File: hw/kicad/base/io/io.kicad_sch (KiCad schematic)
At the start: 13 parts, among them J1 SPI, J10 Conn_02x20_Odd_Even, J11 ADC 2, J12 UART1, J13 Conn_02x20_Odd_Even, J2 PWM, J3 UART2, J4 I2C, J5 PWM, J6 CAN, J7 PWM, J8 PWM, J9 ADC 1

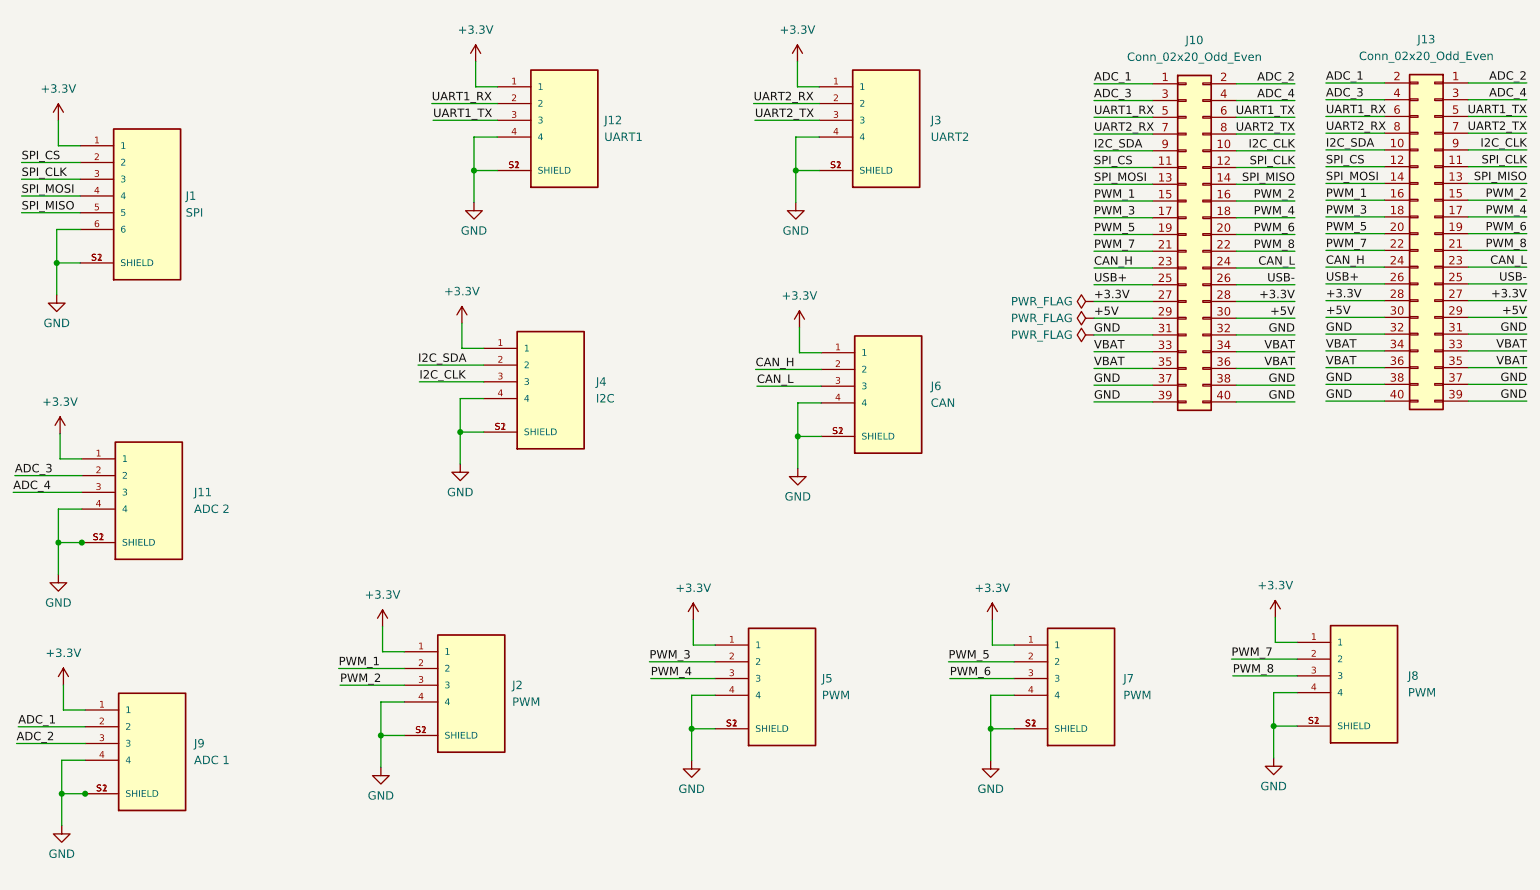
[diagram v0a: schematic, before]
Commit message: 新增陀螺仪小板子
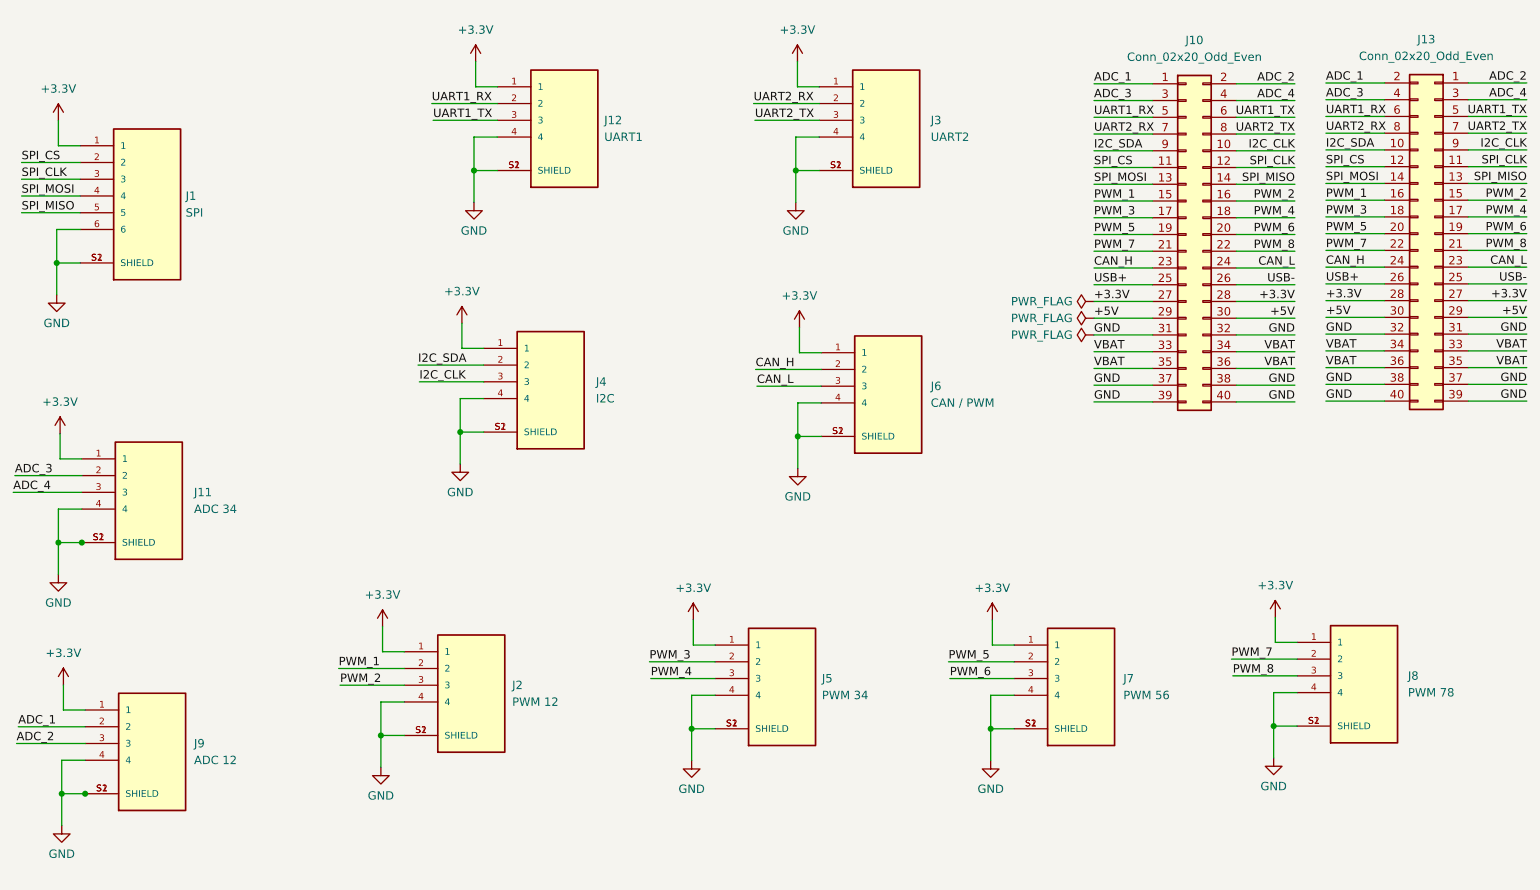
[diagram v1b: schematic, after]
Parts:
- J11: value ADC 2 -> ADC 34
- J2: value PWM -> PWM 12
- J5: value PWM -> PWM 34
- J6: value CAN -> CAN / PWM
- J7: value PWM -> PWM 56
- J8: value PWM -> PWM 78
- J9: value ADC 1 -> ADC 12
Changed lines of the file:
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@@
       (effects (font (size 1.27 1.27)) (justify left))
     )
-    (property "Value" "PWM" (at 158.75 144.5768 0)
+    (property "Value" "PWM 34" (at 158.75 144.5768 0)
       (effects (font (size 1.27 1.27)) (justify left))
     )
@@
       (effects (font (size 1.27 1.27)) (justify left))
     )
-    (property "Value" "ADC 1" (at 63.5 154.432 0)
+    (property "Value" "ADC 12" (at 63.5 154.432 0)
       (effects (font (size 1.27 1.27)) (justify left))
     )
@@
       (effects (font (size 1.27 1.27)) (justify left))
     )
-    (property "Value" "PWM" (at 204.47 144.5768 0)
+    (property "Value" "PWM 56" (at 204.47 144.5768 0)
       (effects (font (size 1.27 1.27)) (justify left))
     )
@@
       (effects (font (size 1.27 1.27)) (justify left))
     )
-    (property "Value" "CAN" (at 175.26 100.2284 0)
+    (property "Value" "CAN / PWM" (at 175.26 100.2284 0)
       (effects (font (size 1.27 1.27)) (justify left))
     )
@@
       (effects (font (size 1.27 1.27)) (justify left))
     )
-    (property "Value" "PWM" (at 111.76 145.5928 0)
+    (property "Value" "PWM 12" (at 111.76 145.5928 0)
       (effects (font (size 1.27 1.27)) (justify left))
     )
@@
       (effects (font (size 1.27 1.27)) (justify left))
     )
-    (property "Value" "PWM" (at 247.65 144.1704 0)
+    (property "Value" "PWM 78" (at 247.65 144.1704 0)
       (effects (font (size 1.27 1.27)) (justify left))
     )
@@
       (effects (font (size 1.27 1.27)) (justify left))
     )
-    (property "Value" "ADC 2" (at 63.5 116.332 0)
-      (effects (font (size 1.27 1.27)) (justify left))
-    )
+    (property "Value" "ADC 34" (at 63.5 116.332 0)
+      (effects (font (size 1.27 1.27)) (justify left))
+    )

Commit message: 更换接口线序
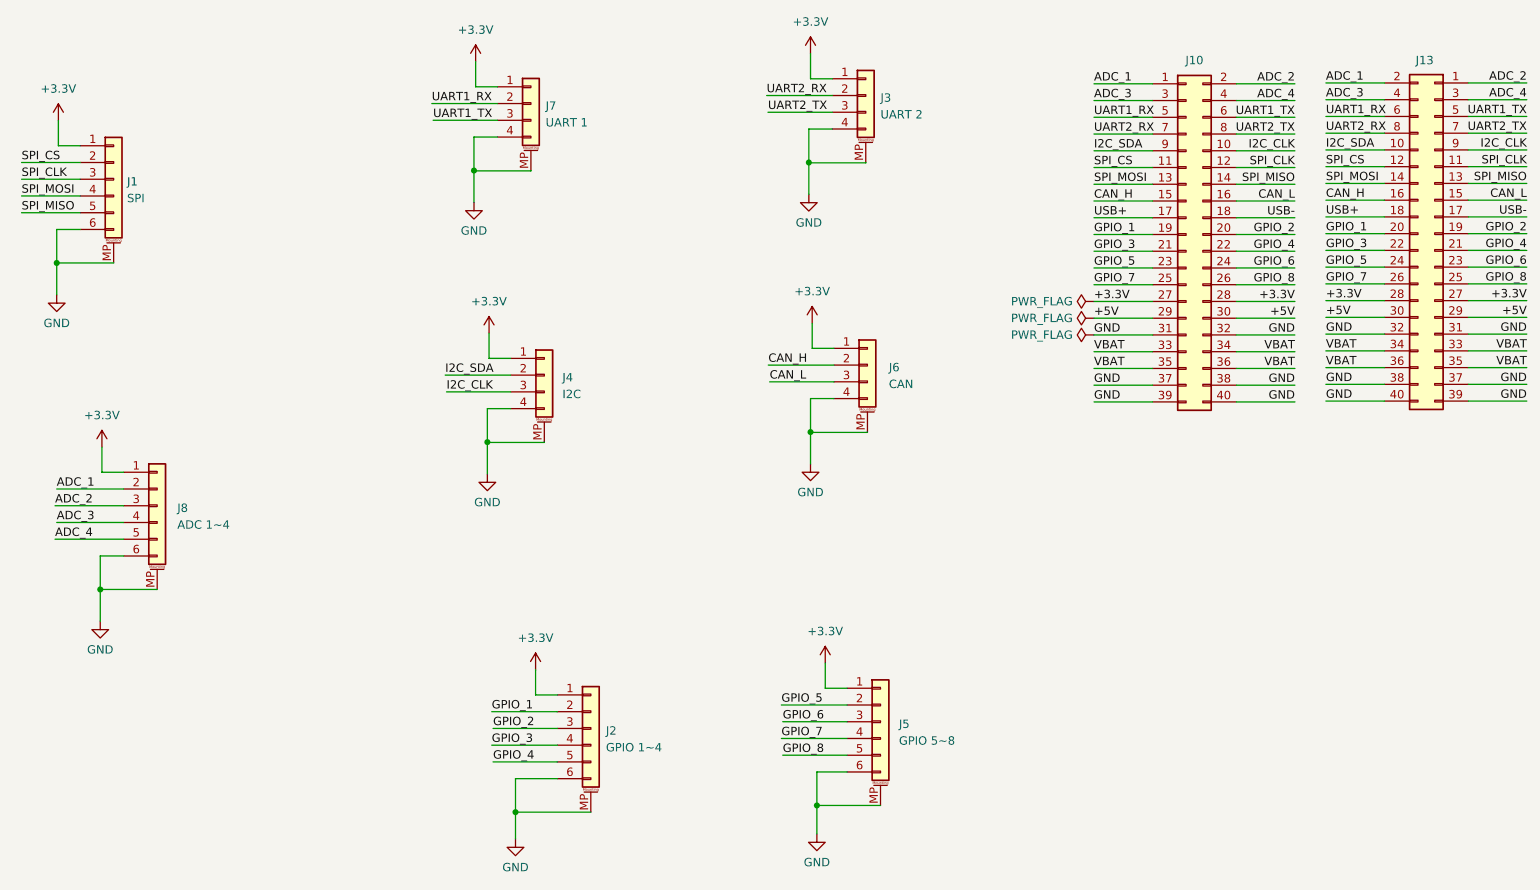
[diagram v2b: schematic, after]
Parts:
- removed J1: SPI, Connector_JST:JST_GH_BM06B-GHS-TBT_1x06-1MP_P1.25mm_Vertical, symbol JST-GHS-1.25-BM06B:BM06B-GHS-TBT(LF)(SN)(N)
- removed J11: ADC 34, Connector_JST:JST_GH_BM04B-GHS-TBT_1x04-1MP_P1.25mm_Vertical, symbol JST-GHS-1.25-BM04B:BM04B-GHS-TBT(LF)(SN)(N)
- removed J12: UART1, Connector_JST:JST_GH_BM04B-GHS-TBT_1x04-1MP_P1.25mm_Vertical, symbol JST-GHS-1.25-BM04B:BM04B-GHS-TBT(LF)(SN)(N)
- removed J2: PWM 12, Connector_JST:JST_GH_BM04B-GHS-TBT_1x04-1MP_P1.25mm_Vertical, symbol JST-GHS-1.25-BM04B:BM04B-GHS-TBT(LF)(SN)(N)
- removed J3: UART2, Connector_JST:JST_GH_BM04B-GHS-TBT_1x04-1MP_P1.25mm_Vertical, symbol JST-GHS-1.25-BM04B:BM04B-GHS-TBT(LF)(SN)(N)
- removed J4: I2C, Connector_JST:JST_GH_BM04B-GHS-TBT_1x04-1MP_P1.25mm_Vertical, symbol JST-GHS-1.25-BM04B:BM04B-GHS-TBT(LF)(SN)(N)
- removed J5: PWM 34, Connector_JST:JST_GH_BM04B-GHS-TBT_1x04-1MP_P1.25mm_Vertical, symbol JST-GHS-1.25-BM04B:BM04B-GHS-TBT(LF)(SN)(N)
- removed J6: CAN / PWM, Connector_JST:JST_GH_BM04B-GHS-TBT_1x04-1MP_P1.25mm_Vertical, symbol JST-GHS-1.25-BM04B:BM04B-GHS-TBT(LF)(SN)(N)
- removed J7: PWM 56, Connector_JST:JST_GH_BM04B-GHS-TBT_1x04-1MP_P1.25mm_Vertical, symbol JST-GHS-1.25-BM04B:BM04B-GHS-TBT(LF)(SN)(N)
- removed J8: PWM 78, Connector_JST:JST_GH_BM04B-GHS-TBT_1x04-1MP_P1.25mm_Vertical, symbol JST-GHS-1.25-BM04B:BM04B-GHS-TBT(LF)(SN)(N)
- removed J9: ADC 12, Connector_JST:JST_GH_BM04B-GHS-TBT_1x04-1MP_P1.25mm_Vertical, symbol JST-GHS-1.25-BM04B:BM04B-GHS-TBT(LF)(SN)(N)
- added J1: SPI, Connector_JST:JST_GH_BM06B-GHS-TBT_1x06-1MP_P1.25mm_Vertical, symbol Connector_Generic_MountingPin:Conn_01x06_MountingPin
- added J2: GPIO 1~4, Connector_JST:JST_GH_BM06B-GHS-TBT_1x06-1MP_P1.25mm_Vertical, symbol Connector_Generic_MountingPin:Conn_01x06_MountingPin
- added J3: UART 2, Connector_JST:JST_GH_BM04B-GHS-TBT_1x04-1MP_P1.25mm_Vertical, symbol Connector_Generic_MountingPin:Conn_01x04_MountingPin
- added J4: I2C, Connector_JST:JST_GH_BM04B-GHS-TBT_1x04-1MP_P1.25mm_Vertical, symbol Connector_Generic_MountingPin:Conn_01x04_MountingPin
- added J5: GPIO 5~8, Connector_JST:JST_GH_BM06B-GHS-TBT_1x06-1MP_P1.25mm_Vertical, symbol Connector_Generic_MountingPin:Conn_01x06_MountingPin
- added J6: CAN, Connector_JST:JST_GH_BM04B-GHS-TBT_1x04-1MP_P1.25mm_Vertical, symbol Connector_Generic_MountingPin:Conn_01x04_MountingPin
- added J7: UART 1, Connector_JST:JST_GH_BM04B-GHS-TBT_1x04-1MP_P1.25mm_Vertical, symbol Connector_Generic_MountingPin:Conn_01x04_MountingPin
- added J8: ADC 1~4, Connector_JST:JST_GH_BM06B-GHS-TBT_1x06-1MP_P1.25mm_Vertical, symbol Connector_Generic_MountingPin:Conn_01x06_MountingPin
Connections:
- net PWM_1 is gone; now on net CAN_H: J10.15 (Pin_15), J13.16 (Pin_16)
- net PWM_2 is gone; now on net CAN_L: J10.16 (Pin_16), J13.15 (Pin_15)
- net PWM_3 is gone; now on net USB+: J10.17 (Pin_17), J13.18 (Pin_18)
- net PWM_4 is gone; now on net USB-: J10.18 (Pin_18), J13.17 (Pin_17)
- net +3.3V: now also J1.1 (Pin_1), J2.1 (Pin_1), J3.1 (Pin_1), J4.1 (Pin_1), J5.1 (Pin_1), J6.1 (Pin_1), J7.1 (Pin_1), J8.1 (Pin_1)
- net ADC_1: now also J8.2 (Pin_2)
- net ADC_2: now also J8.3 (Pin_3)
- net ADC_3: now also J8.4 (Pin_4)
- net ADC_4: now also J8.5 (Pin_5)
- net CAN_H: now also J6.2 (Pin_2); no longer J10.23 (Pin_23), J13.24 (Pin_24)
- net CAN_L: now also J6.3 (Pin_3); no longer J10.24 (Pin_24), J13.23 (Pin_23)
- net GND: now also J1.6 (Pin_6), J1.MP (MountPin), J2.6 (Pin_6), J2.MP (MountPin), J3.4 (Pin_4), J3.MP (MountPin), J4.4 (Pin_4), J4.MP (MountPin), J5.6 (Pin_6), J5.MP (MountPin), J6.4 (Pin_4), J6.MP (MountPin), J7.4 (Pin_4), J7.MP (MountPin), J8.6 (Pin_6), J8.MP (MountPin)
- net I2C_CLK: now also J4.3 (Pin_3)
- net I2C_SDA: now also J4.2 (Pin_2)
- net SPI_CLK: now also J1.3 (Pin_3)
- net SPI_CS: now also J1.2 (Pin_2)
- net SPI_MISO: now also J1.5 (Pin_5)
- net SPI_MOSI: now also J1.4 (Pin_4)
- net UART1_RX: now also J7.2 (Pin_2)
- net UART1_TX: now also J7.3 (Pin_3)
- net UART2_RX: now also J3.2 (Pin_2)
- net UART2_TX: now also J3.3 (Pin_3)
- net USB+: no longer J10.25 (Pin_25), J13.26 (Pin_26)
- net USB-: no longer J10.26 (Pin_26), J13.25 (Pin_25)
- net PWM_5 renamed GPIO_1
- net GPIO_1: now also J2.2 (Pin_2)
- net PWM_6 renamed GPIO_2
- net GPIO_2: now also J2.3 (Pin_3)
- net PWM_7 renamed GPIO_3
- net GPIO_3: now also J2.4 (Pin_4)
- net PWM_8 renamed GPIO_4
- net GPIO_4: now also J2.5 (Pin_5)
- new net GPIO_5: J10.23 (Pin_23), J13.24 (Pin_24), J5.2 (Pin_2)
- new net GPIO_6: J10.24 (Pin_24), J13.23 (Pin_23), J5.3 (Pin_3)
- new net GPIO_7: J10.25 (Pin_25), J13.26 (Pin_26), J5.4 (Pin_4)
- new net GPIO_8: J10.26 (Pin_26), J13.25 (Pin_25), J5.5 (Pin_5)

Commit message: 尽力改成40mmx40mm
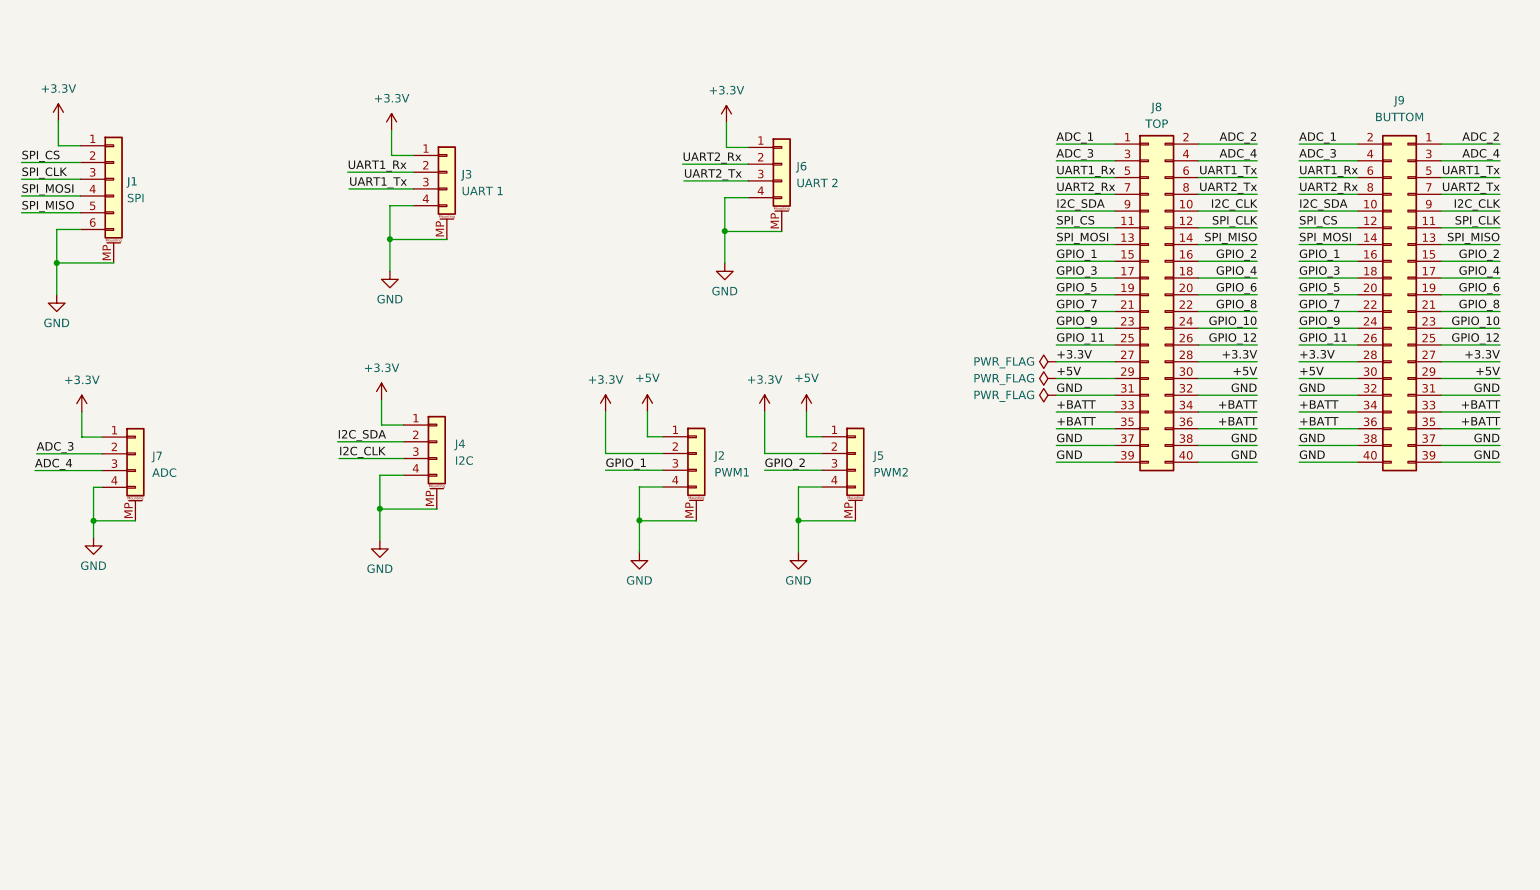
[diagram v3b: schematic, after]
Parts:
- removed J10, J13: Conn_02x20_Odd_Even, Connector_PinHeader_1.27mm:PinHeader_2x20_P1.27mm_Vertical_SMD, symbol Connector_Generic:Conn_02x20_Odd_Even
- removed J2: GPIO 1~4, Connector_JST:JST_GH_BM06B-GHS-TBT_1x06-1MP_P1.25mm_Vertical, symbol Connector_Generic_MountingPin:Conn_01x06_MountingPin
- removed J5: GPIO 5~8, Connector_JST:JST_GH_BM06B-GHS-TBT_1x06-1MP_P1.25mm_Vertical, symbol Connector_Generic_MountingPin:Conn_01x06_MountingPin
- removed J6: CAN, Connector_JST:JST_GH_BM04B-GHS-TBT_1x04-1MP_P1.25mm_Vertical, symbol Connector_Generic_MountingPin:Conn_01x04_MountingPin
- removed J8: ADC 1~4, Connector_JST:JST_GH_BM06B-GHS-TBT_1x06-1MP_P1.25mm_Vertical, symbol Connector_Generic_MountingPin:Conn_01x06_MountingPin
- added J2: PWM1, Connector_JST:JST_GH_BM04B-GHS-TBT_1x04-1MP_P1.25mm_Vertical, symbol Connector_Generic_MountingPin:Conn_01x04_MountingPin
- added J5: PWM2, Connector_JST:JST_GH_BM04B-GHS-TBT_1x04-1MP_P1.25mm_Vertical, symbol Connector_Generic_MountingPin:Conn_01x04_MountingPin
- added J7: ADC, Connector_JST:JST_GH_BM04B-GHS-TBT_1x04-1MP_P1.25mm_Vertical, symbol Connector_Generic_MountingPin:Conn_01x04_MountingPin
- added J8: TOP, Connector_PinHeader_1.27mm:PinHeader_2x20_P1.27mm_Vertical_SMD, symbol Connector_Generic:Conn_02x20_Odd_Even
- added J9: BUTTOM, Connector_PinHeader_1.27mm:PinHeader_2x20_P1.27mm_Vertical_SMD, symbol Connector_Generic:Conn_02x20_Odd_Even
- renumbered J7 to J3, J3 to J6
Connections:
- net +3.3V: now also J2.2 (Pin_2), J5.2 (Pin_2), J7.1 (Pin_1), J8.27 (Pin_27), J8.28 (Pin_28), J9.27 (Pin_27), J9.28 (Pin_28)
- net +5V: now also J2.1 (Pin_1), J5.1 (Pin_1), J8.29 (Pin_29), J8.30 (Pin_30), J9.29 (Pin_29), J9.30 (Pin_30)
- net ADC_1: now also J8.1 (Pin_1), J9.2 (Pin_2)
- net ADC_2: now also J8.2 (Pin_2), J9.1 (Pin_1)
- net ADC_3: now also J7.2 (Pin_2), J8.3 (Pin_3), J9.4 (Pin_4)
- net ADC_4: now also J7.3 (Pin_3), J8.4 (Pin_4), J9.3 (Pin_3)
- net GND: now also J2.4 (Pin_4), J2.MP (MountPin), J5.4 (Pin_4), J5.MP (MountPin), J7.4 (Pin_4), J7.MP (MountPin), J8.31 (Pin_31), J8.32 (Pin_32), J8.37 (Pin_37), J8.38 (Pin_38), J8.39 (Pin_39), J8.40 (Pin_40), J9.31 (Pin_31), J9.32 (Pin_32), J9.37 (Pin_37), J9.38 (Pin_38), J9.39 (Pin_39), J9.40 (Pin_40)
- net GPIO_1: now also J2.3 (Pin_3), J8.15 (Pin_15), J9.16 (Pin_16)
- net GPIO_2: now also J5.3 (Pin_3), J8.16 (Pin_16), J9.15 (Pin_15)
- net GPIO_3: now also J8.17 (Pin_17), J9.18 (Pin_18)
- net GPIO_4: now also J8.18 (Pin_18), J9.17 (Pin_17)
- net GPIO_5: now also J8.19 (Pin_19), J9.20 (Pin_20)
- net GPIO_6: now also J8.20 (Pin_20), J9.19 (Pin_19)
- net GPIO_7: now also J8.21 (Pin_21), J9.22 (Pin_22)
- net GPIO_8: now also J8.22 (Pin_22), J9.21 (Pin_21)
- net I2C_CLK: now also J8.10 (Pin_10), J9.9 (Pin_9)
- net I2C_SDA: now also J8.9 (Pin_9), J9.10 (Pin_10)
- net SPI_CLK: now also J8.12 (Pin_12), J9.11 (Pin_11)
- net SPI_CS: now also J8.11 (Pin_11), J9.12 (Pin_12)
- net SPI_MISO: now also J8.14 (Pin_14), J9.13 (Pin_13)
- net SPI_MOSI: now also J8.13 (Pin_13), J9.14 (Pin_14)
- net UART1_RX renamed UART1_Rx
- net UART1_Rx: now also J8.5 (Pin_5), J9.6 (Pin_6)
- net UART1_TX renamed UART1_Tx
- net UART1_Tx: now also J8.6 (Pin_6), J9.5 (Pin_5)
- net UART2_RX renamed UART2_Rx
- net UART2_Rx: now also J8.7 (Pin_7), J9.8 (Pin_8)
- net UART2_TX renamed UART2_Tx
- net UART2_Tx: now also J8.8 (Pin_8), J9.7 (Pin_7)
- new net +BATT: J8.33 (Pin_33), J8.34 (Pin_34), J8.35 (Pin_35), J8.36 (Pin_36), J9.33 (Pin_33), J9.34 (Pin_34), J9.35 (Pin_35), J9.36 (Pin_36)
- new net GPIO_10: J8.24 (Pin_24), J9.23 (Pin_23)
- new net GPIO_11: J8.25 (Pin_25), J9.26 (Pin_26)
- new net GPIO_12: J8.26 (Pin_26), J9.25 (Pin_25)
- new net GPIO_9: J8.23 (Pin_23), J9.24 (Pin_24)
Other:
- moved on the sheet: J3, J4, J6
